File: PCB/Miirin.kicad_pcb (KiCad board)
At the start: 2 copper layers, 79.5 x 93.5 mm, 29 parts, among them J1 Conn_01x04_Socket, J2 AudioJack3_Switch, Q1 Q_PMOS_GDS, SW1 SW_Push, SW2 SW_Push, SW3 SW_Push, SW4 SW_Push, SW5 SW_Push, SW6 RotaryEncoder, U1 XIAO-ESP32-S3-THT, U2 DFR0768, U3 PCF8574P

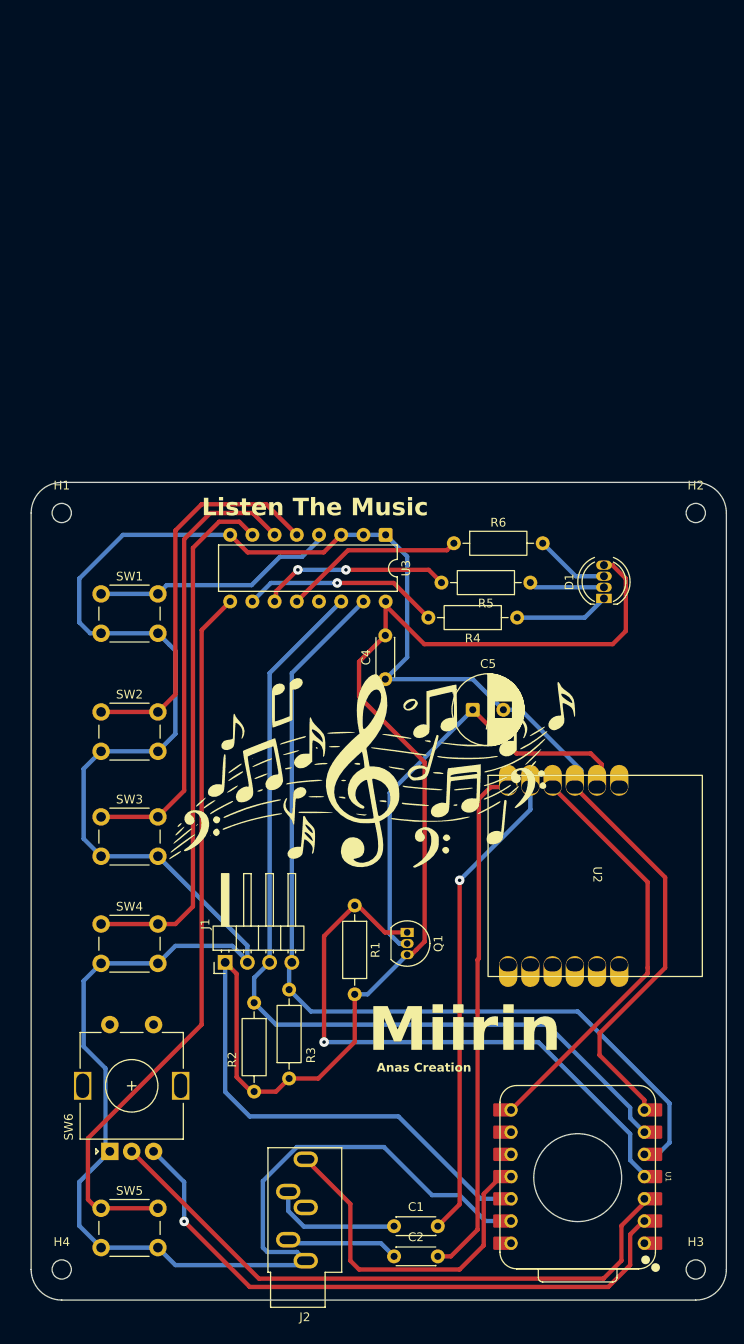
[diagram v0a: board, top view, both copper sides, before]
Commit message: Updated the PCB design and CAD file with the new one. Added .stl file of the case. Updated the BOM in BOM.csv and README.md
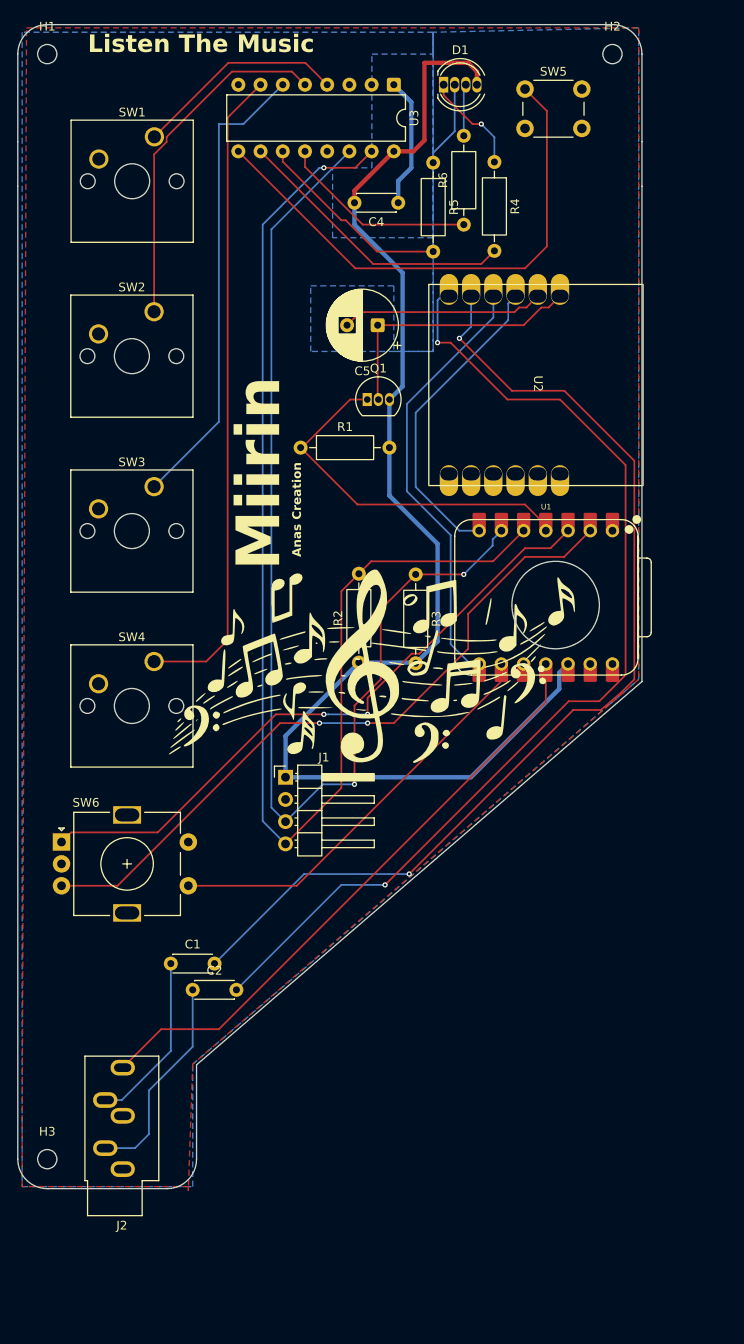
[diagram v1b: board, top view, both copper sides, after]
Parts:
- removed H4: MountingHole, MountingHole:MountingHole_2.2mm_M2
- SW1, SW2, SW3, SW4: footprint Button_Switch_THT:SW_PUSH_6mm -> Button_Switch_Keyboard:SW_Cherry_MX_1.00u_PCB
- SW6: value RotaryEncoder -> RotaryEncoder_Switch
- moved SW5 136.8 mm to (79.5, 49.0)
- moved H3 75.2 mm to (24.9, 171.4)
- moved U1 66.3 mm to (81.9, 107.1), turned to 0 degrees
- moved D1 61.5 mm to (70.2, 48.5), turned to 0 degrees
- moved Q1 61.1 mm to (61.5, 84.5), turned to 0 degrees
- moved U2 56.5 mm to (83.5, 72.7)
- moved G*** 56.4 mm to (79.9, 82.8)
- moved C4 54.5 mm to (65.0, 62.0), turned to 180 degrees
- moved H2 53.3 mm to (89.5, 45.0)
- moved R1 52.7 mm to (53.8, 90.0), turned to 0 degrees
- moved SW1 52.6 mm to (37.1, 54.5)
- moved H1 52.5 mm to (24.9, 45.0)
- moved R3 52.3 mm to (67.0, 104.5)
- moved R4 52.2 mm to (76.0, 57.3), turned to -90 degrees
- moved U3 51.5 mm to (64.5, 48.5)
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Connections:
- SW6 pad A: GND -> /RoEn C
- SW6 pad C: /RoEn C -> GND
- SW6 pad S1: (no net) -> /RoEn S1
- SW6 pad S2: (no net) -> GND
- U1 pad 9: unconnected-(U1-D8-Pad9)_1 -> /RoEn S1
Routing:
- net GND: track 284.6 -> 38.2 mm
- net Net-(U2-DACR): track 54.6 -> 117.9 mm, vias 1 -> 2
- net Net-(U2-DACL): track 59.0 -> 117.1 mm, vias 0 -> 2
- net /RoEn S1: track 0.00 -> 46.5 mm
- net /SDA: track 104.7 -> 143.1 mm, vias 0 -> 1
- net +3V3: track 182.0 -> 149.6 mm
- net /D10: track 40.4 -> 69.1 mm
- net /D3: track 69.2 -> 42.2 mm, vias 1 -> 0
- net /SCL: track 102.3 -> 128.3 mm, vias 0 -> 2
- net /SW5: track 83.5 -> 60.9 mm
- net /DFP Vin: track 51.1 -> 30.8 mm
- net /SW4: track 61.0 -> 74.5 mm
- net /TX: track 46.4 -> 35.9 mm
- net Net-(C2-Pad1): track 12.9 -> 23.2 mm
- net /R: track 22.6 -> 32.7 mm, vias 1 -> 0
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- added copper zone on F.Cu, net (none)
- added copper zone on B.Cu, net GND
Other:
- board size 79.5 x 93.5 mm -> 71.4 x 133.1 mm
